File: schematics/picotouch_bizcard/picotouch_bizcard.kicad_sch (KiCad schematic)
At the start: 48 parts, among them J2 AudioJack4, SW1 Capacitive Button, SW10 Capacitive Button, SW11 Capacitive Button, SW12 Capacitive Button, SW2 Capacitive Button, SW3 Capacitive Button, SW4 Capacitive Button, SW5 Capacitive Button, SW6 Capacitive Button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

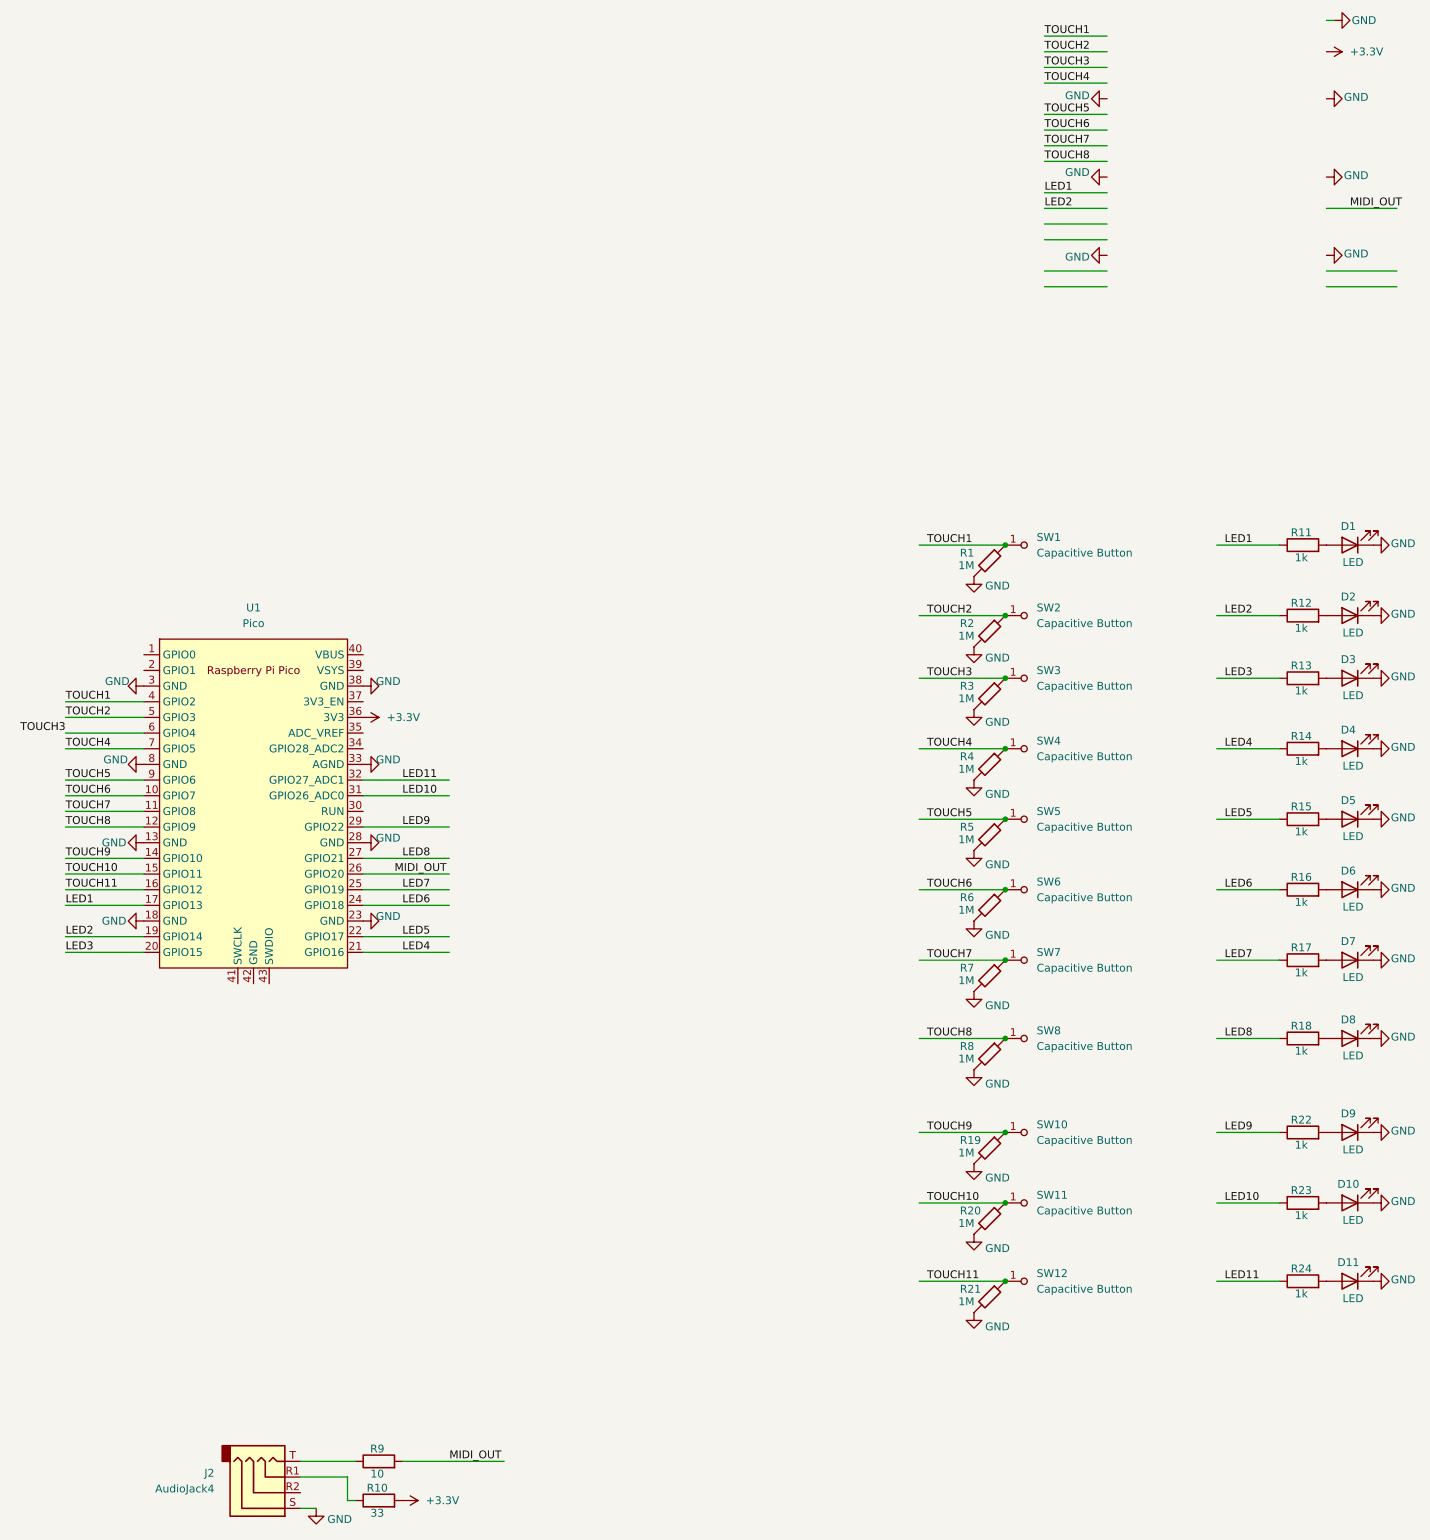
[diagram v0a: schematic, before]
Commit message: added tx/rx test points and mounting hole
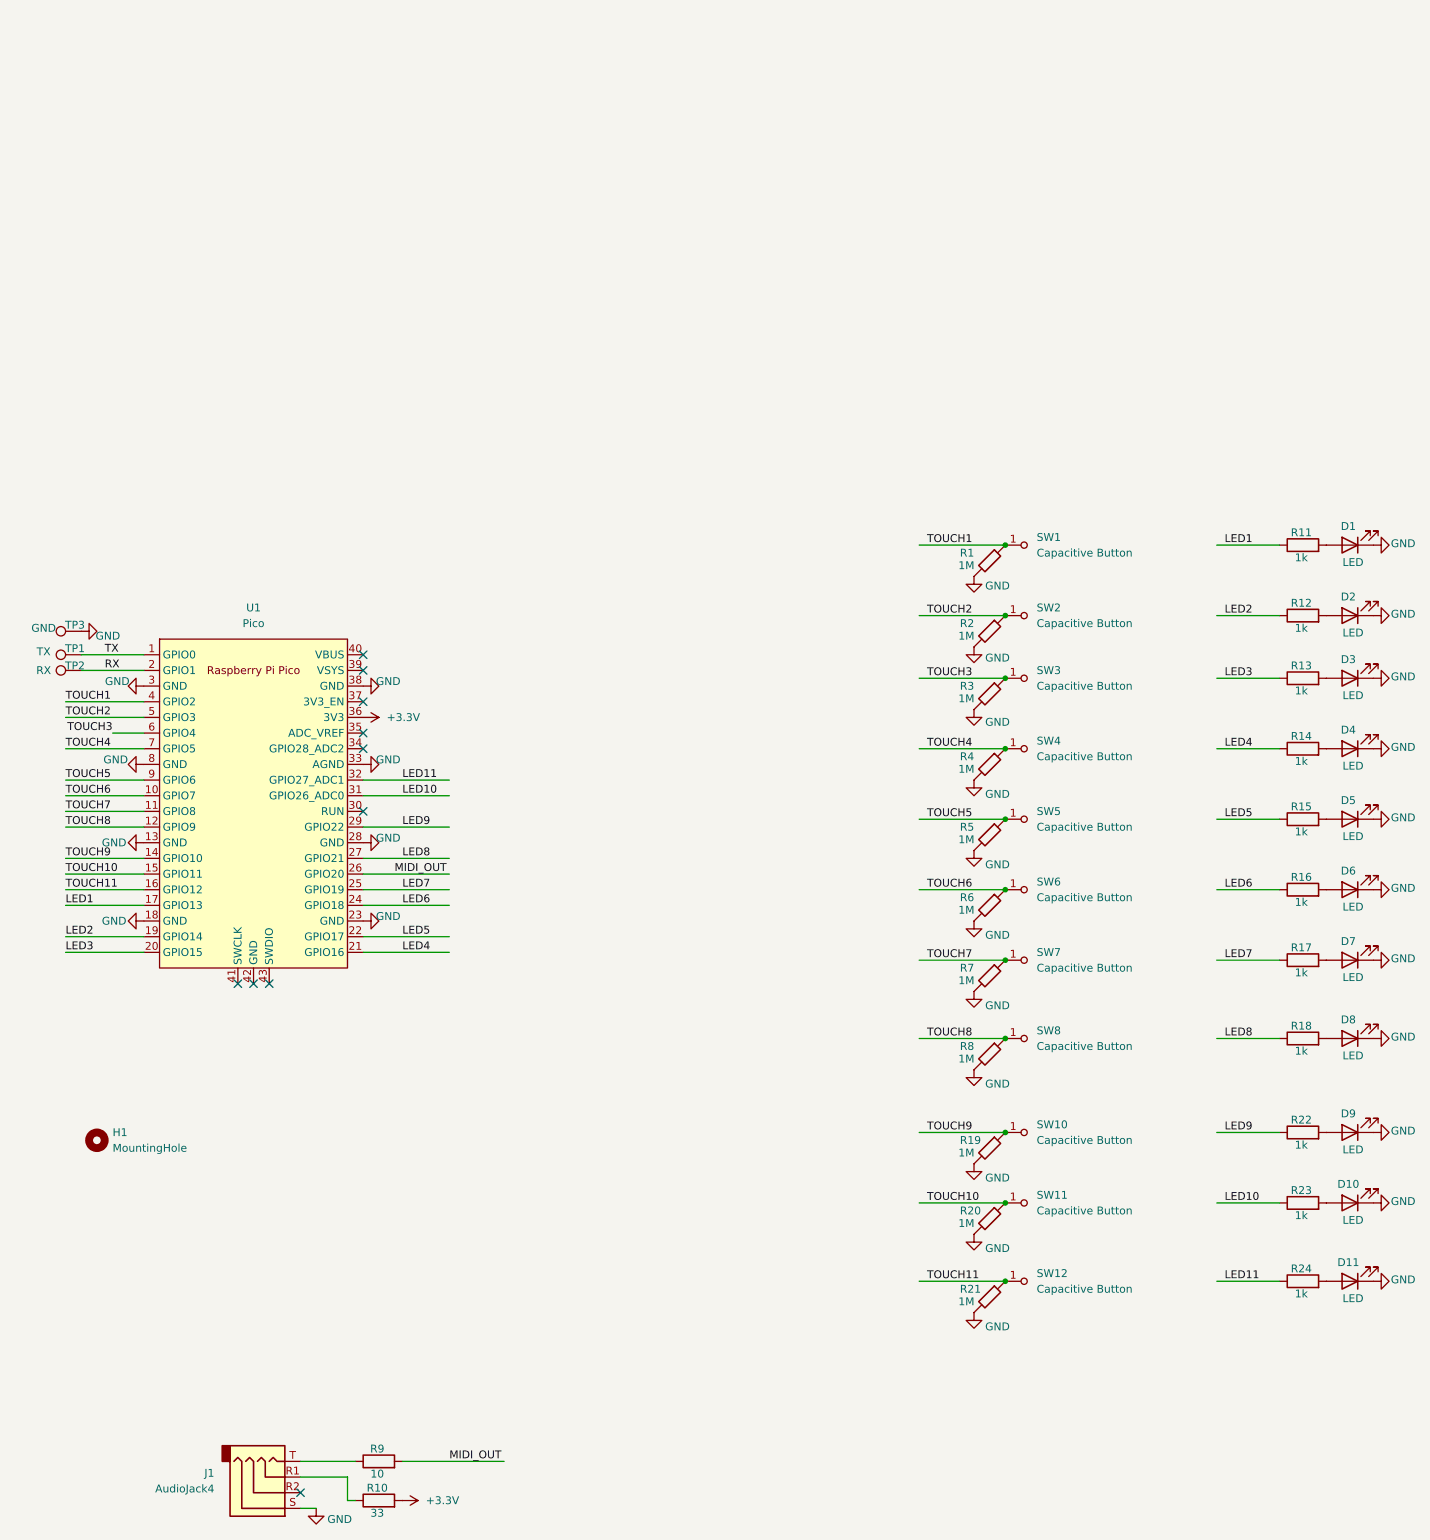
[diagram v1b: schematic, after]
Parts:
- added H1: MountingHole, MountingHole:MountingHole_2.5mm, symbol Mechanical:MountingHole
- added TP1: TX, TestPoint:TestPoint_Pad_D2.0mm, symbol Connector:TestPoint
- added TP2: RX, TestPoint:TestPoint_Pad_D2.0mm, symbol Connector:TestPoint
- added TP3: GND, TestPoint:TestPoint_Pad_D2.0mm, symbol Connector:TestPoint
- SW1: footprint todbot_stuff:Pad-CapacitiveTouch-SparkFun -> SparkFun-Switch:Pad-CapacitiveTouch; now left out of the parts list
- SW10, SW11, SW12, SW2, SW3, SW4, SW5, SW6, SW7, SW8: now left out of the parts list
- renumbered J2 to J1
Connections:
- net GND: now also TP3.1
- net TX: now reaches U1.1 (GPIO0)
- net TX: now also TP1.1
- net RX: now reaches U1.2 (GPIO1)
- net RX: now also TP2.1
- no-connect marks 0 -> 10

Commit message: submit to fab
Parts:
- TP1, TP2, TP3: now left out of the parts list
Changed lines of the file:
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@@
 		(unit 1)
 		(exclude_from_sim no)
-		(in_bom yes)
+		(in_bom no)
 		(on_board yes)
 		(dnp no)
@@
 		(unit 1)
 		(exclude_from_sim no)
-		(in_bom yes)
+		(in_bom no)
 		(on_board yes)
 		(dnp no)
@@
 		(unit 1)
 		(exclude_from_sim no)
-		(in_bom yes)
+		(in_bom no)
 		(on_board yes)
 		(dnp no)
